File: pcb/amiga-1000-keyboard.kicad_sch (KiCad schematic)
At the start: 113 parts, among them J1 KEYBOARD, Q1 NPN, SW1 ESC, SW10 F9, SW11 F10, SW12 HELP, SW13 `, SW14 1, SW15 2, SW16 3, SW17 4, SW18 5, SW19 6, SW2 F1, SW20 7, SW21 8, SW22 9, SW23 0, SW24 -, SW25 =, SW26 \, SW27 UP, SW28 TAB, SW29 Q, SW3 F2, SW30 W, SW31 E, SW32 R, SW33 T, SW34 Y, SW35 U, SW36 I, SW37 O, SW38 P, SW39 [, SW4 F3, SW40 ], SW41 RETURN, SW42 LEFT, SW43 CAPS LOCK, SW44 A, SW45 S, SW46 D, SW47 F, SW48 G, SW49 H, SW5 F4, SW50 J, SW51 K, SW52 L, SW53 ;, SW54 ', SW55 (RET) INTL, SW56 DEL, SW57 RIGHT, SW58 L SHIFT INTL, SW59 Z, SW6 F5, SW60 X, SW61 C, SW62 V, SW63 B, SW64 N, SW65 M, SW66 ,, SW67 ., SW68 /, SW69 SPACE, SW7 F6, SW70 BACKSPACE, SW71 DOWN, SW72 KP 9, SW73 KP 6, SW74 KP 3, SW75 KP ., SW76 KP 8, SW77 KP 5, SW78 KP 2, SW79 KP ENTER, SW8 F7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

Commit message: assign footprints, set the 3mhz crystal and add the iso shift switch.
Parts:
- added SW92: L SHIFT ISO, amiga1000:Mitsumi_A1000_Switch, symbol Switch:SW_Push
- C1, C2, C3, C4, C6, C7, C9: footprint (none) -> Capacitor_THT:C_Disc_D5.0mm_W2.5mm_P5.00mm
- C5: value 1uF -> 1uF 25V tant; footprint (none) -> Capacitor_THT:CP_Radial_Tantal_D4.5mm_P2.50mm; symbol Device:C -> Device:C_Polarized
- C8: footprint (none) -> Capacitor_THT:CP_Radial_D5.0mm_P2.00mm
- D1: footprint (none) -> Diode_THT:D_DO-35_SOD27_P7.62mm_Horizontal
- D2: footprint (none) -> amiga1000:Mitsumi_A1000_CapsLock_LED
- FB1, FB2, FB3: footprint (none) -> Inductor_THT:L_Axial_L9.5mm_D4.0mm_P12.70mm_Horizontal_Fastron_SMCC
- J1: footprint (none) -> Connector_PinHeader_2.54mm:PinHeader_1x04_P2.54mm_Vertical
- Q1: footprint (none) -> amiga1000:TO-92_Inline_ECB
- R1, R2, R3: footprint (none) -> Resistor_THT:R_Axial_DIN0207_L6.3mm_D2.5mm_P10.16mm_Horizontal
- SW1, SW10, SW11, SW12, SW13, SW14, SW15, SW16, SW17, SW18, SW19, SW2, SW20, SW21, SW22, SW23, SW24, SW25, SW26, SW27, SW28, SW29, SW3, SW30, SW31, SW32, SW33, SW34, SW35, SW36, SW37, SW38, SW39, SW4, SW40, SW41, SW42, SW43, SW44, SW45, SW46, SW47, SW48, SW49, SW5, SW50, SW51, SW52, SW53, SW54, SW56, SW57, SW59, SW6, SW60, SW61, SW62, SW63, SW64, SW65, SW66, SW67, SW68, SW69, SW7, SW70, SW71, SW72, SW73, SW74, SW75, SW76, SW77, SW78, SW79, SW8, SW80, SW81, SW82, SW83, SW84, SW85, SW86, SW87, SW88, SW89, SW9, SW90, SW91: footprint (none) -> amiga1000:Mitsumi_A1000_Switch
- SW55, SW58: footprint (none) -> amiga1000:Mitsumi_A1000_Switch; now not fitted
- U2: footprint (none) -> Package_DIP:DIP-14_W7.62mm
- Y1: value XTAL -> 3.000MHz; footprint (none) -> Crystal:Crystal_HC49-U_Vertical
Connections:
- net GND: now also SW92.2
- net PB4: now also SW92.1
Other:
- note added: "3.000 MHz: not marked on the drawing, read from the crystal on an assembled board."
- note removed: "Crystal frequency not marked on the drawing - verify on an original board."

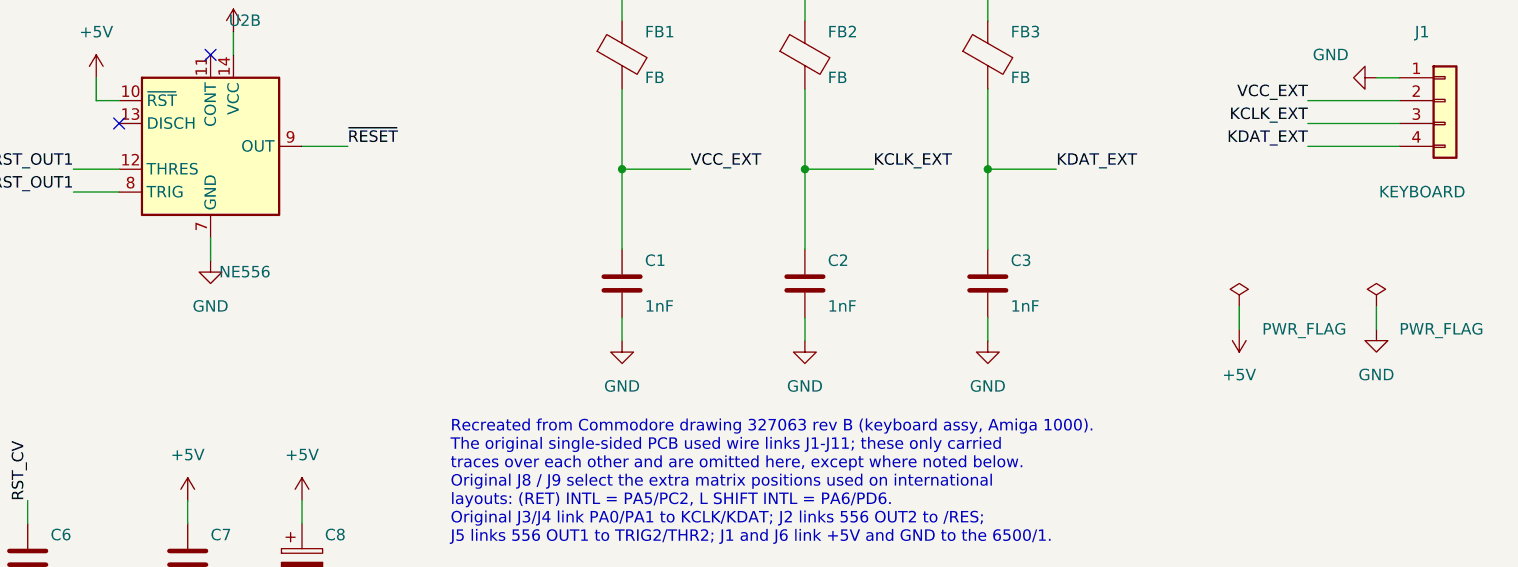
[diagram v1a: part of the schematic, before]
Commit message: mark the unfitted cable filter caps c1-c3 do not populate.
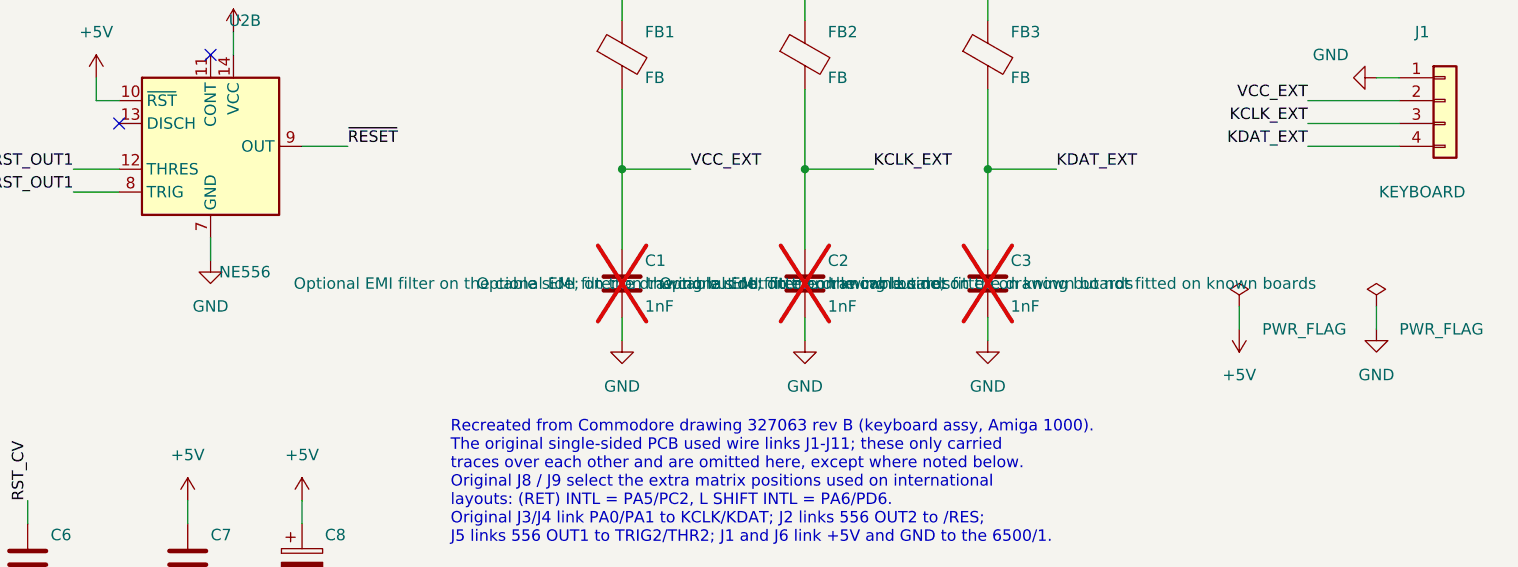
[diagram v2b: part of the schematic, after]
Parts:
- C1, C2, C3: now not fitted
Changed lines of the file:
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@@
 		(on_board yes)
 		(in_pos_files yes)
-		(dnp no)
+		(dnp yes)
 		(property "Reference" "C2"
 			(at 325.12 218.44 0)
@@
 			)
 		)
-		(property "Description" ""
+		(property "Description" "Optional EMI filter on the cable side; on the drawing but not fitted on known boards"
 			(at 322.58 220.98 0)
 			(show_name no)
@@
 		(on_board yes)
 		(in_pos_files yes)
-		(dnp no)
+		(dnp yes)
 		(property "Reference" "C3"
 			(at 345.44 218.44 0)
@@
 			)
 		)
-		(property "Description" ""
+		(property "Description" "Optional EMI filter on the cable side; on the drawing but not fitted on known boards"
 			(at 342.9 220.98 0)
 			(show_name no)
@@
 		(on_board yes)
 		(in_pos_files yes)
-		(dnp no)
+		(dnp yes)
 		(property "Reference" "C1"
 			(at 304.8 218.44 0)
@@
 			)
 		)
-		(property "Description" ""
+		(property "Description" "Optional EMI filter on the cable side; on the drawing but not fitted on known boards"
 			(at 302.26 220.98 0)
 			(show_name no)

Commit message: add part fields and a bom generated from the schematic.
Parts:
- added H1, H2, H3, H4, H5, H6, H7, H8, H9: Plate GND, amiga1000:MountingHole_3.8mm_Plate_GND, symbol Mechanical:MountingHole_Pad
- C1, C2, C3: Part (none) -> 1nF 50V ceramic disc, 5 mm
- C4, C7: Part (none) -> 100nF 50V ceramic disc, 5 mm
- C5: Part (none) -> 1uF 25V tantalum, 2.5 mm
- C6: Part (none) -> 10nF 50V ceramic disc, 5 mm
- C8: Part (none) -> 47uF 16V electrolytic, 5 mm dia, 2 mm
- C9: Part (none) -> 22pF 50V C0G ceramic disc, 5 mm
- D1: Part (none) -> 1N4148 small-signal diode, DO-35
- D2: Part (none) -> LED built into the Caps Lock switch (no separate part)
- FB1, FB2, FB3: Part (none) -> Axial ferrite bead, e.g. Fair-Rite 2743001112
- J1: Part (none) -> Original 4-wire cable soldered in (or a 1x4 2.54 mm header)
- Q1: value NPN -> 2SC2021; footprint amiga1000:TO-92_Inline_ECB -> amiga1000:TO-92_Inline_Wide_ECB; Part (none) -> 2SC2021 (Rohm SPT, original) or 2SC1815/KSC1815 TO-92; any 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
- R1: Part (none) -> 150R 1/4W axial
- R2: Part (none) -> 510K 1/4W axial
- R3: Part (none) -> 560K 1/4W axial
- SW1, SW10, SW11, SW12, SW13, SW14, SW15, SW16, SW17, SW18, SW19, SW2, SW20, SW21, SW22, SW23, SW24, SW25, SW26, SW27, SW28, SW29, SW3, SW30, SW31, SW32, SW33, SW34, SW35, SW36, SW37, SW38, SW39, SW4, SW40, SW41, SW42, SW43, SW44, SW45, SW46, SW47, SW48, SW49, SW5, SW50, SW51, SW52, SW53, SW54, SW55, SW56, SW57, SW58, SW59, SW6, SW60, SW61, SW62, SW63, SW64, SW65, SW66, SW67, SW68, SW69, SW7, SW70, SW71, SW72, SW73, SW74, SW75, SW76, SW77, SW78, SW79, SW8, SW80, SW81, SW82, SW83, SW84, SW85, SW86, SW87, SW88, SW89, SW9, SW90, SW91, SW92: Part (none) -> Mitsumi standard mechanical Type 2 (KCT) keyswitch, salvaged
- U1: Part (none) -> Commodore 6500/1 keyboard controller, salvaged from an A100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
- U2: Part (none) -> NE556N dual timer, DIP-14
- Y1: Part (none) -> 3.000 MHz crystal, HC-49/U
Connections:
- net GND: now also H1.1, H2.1, H3.1, H4.1, H5.1, H6.1, H7.1, H8.1, H9.1
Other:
- note added: "Plate screw holes: plated, tied to GND to ground the steel key plate"

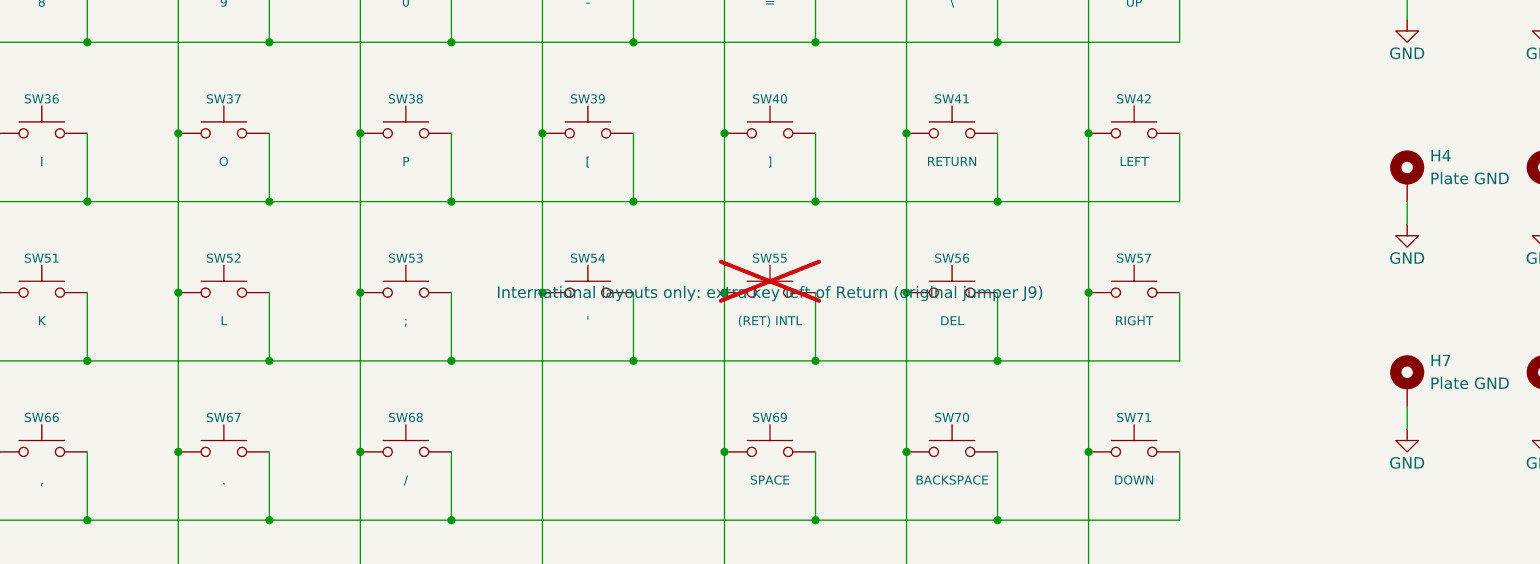
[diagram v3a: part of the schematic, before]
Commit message: turn the return switch round and fit sw55 as the dummy support housing.
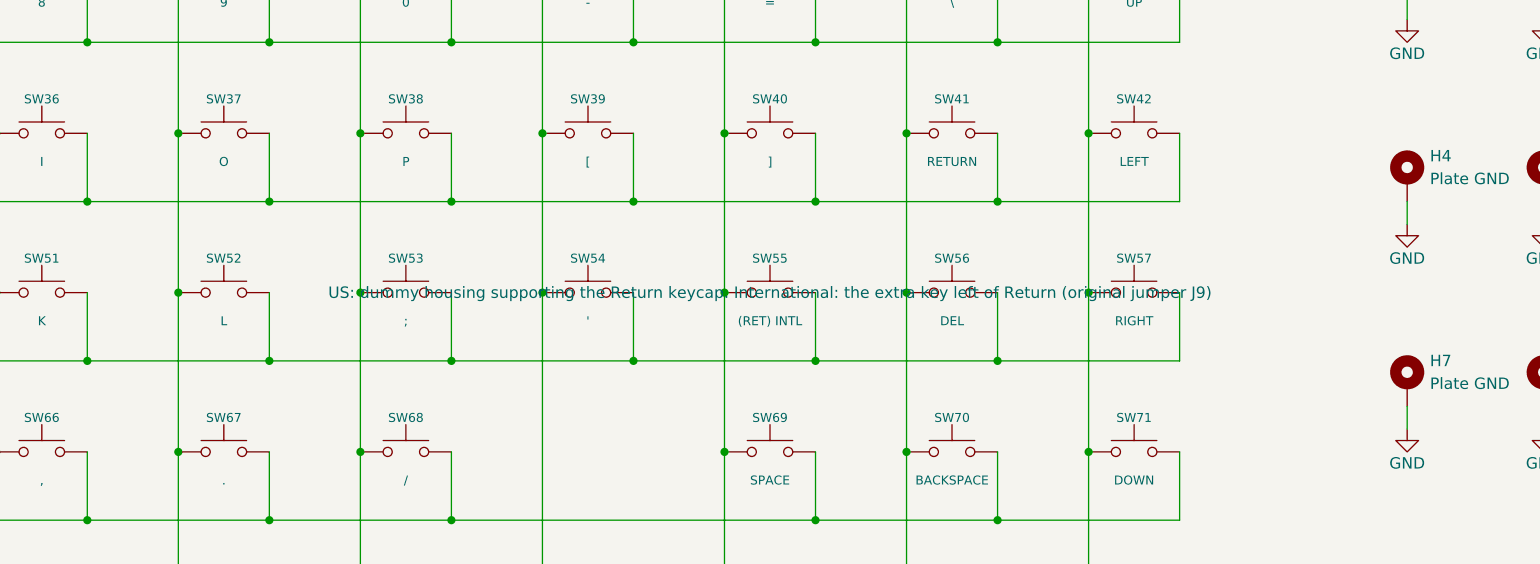
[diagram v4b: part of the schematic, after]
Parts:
- D1: Part 1N4148 small-signal diode, DO-35 -> 1N4148 small-signal diode, DO-35 (original: unmarked glass,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
- SW55: Part Mitsumi standard mechanical Type 2 (KCT) keyswitch, salvaged -> Dummy Mitsumi housing (one leg, no spring) supporting the R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; now fitted
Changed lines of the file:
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@@
 		(on_board yes)
 		(in_pos_files yes)
-		(dnp yes)
+		(dnp no)
 		(property "Reference" "SW55"
 			(at 289.56 87.63 0)
@@
 			)
 		)
-		(property "Description" "International layouts only: extra key left of Return (original jumper J9)"
+		(property "Description" "US: dummy housing supporting the Return keycap. International: the extra key left of Return (original jumper J9)"
 			(at 289.56 91.44 0)
 			(show_name no)
@@
 			)
 		)
-		(property "Part" "Mitsumi standard mechanical Type 2 (KCT) keyswitch, salvaged"
+		(property "Part" "Dummy Mitsumi housing (one leg, no spring) supporting the Return keycap on US layouts; a real switch on international layouts"
 			(at 289.56 91.44 0)
 			(hide yes)
@@
 			)
 		)
-		(property "Part" "1N4148 small-signal diode, DO-35"
+		(property "Part" "1N4148 small-signal diode, DO-35 (original: unmarked glass, yellow cathode band, likely a 1S1588)"
 			(at 170.18 251.46 0)
 			(hide yes)

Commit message: lay y1 flat on the board, can towards the keys, as on the original.
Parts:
- Y1: footprint Crystal:Crystal_HC49-U_Vertical -> Crystal:Crystal_HC49-U_Horizontal
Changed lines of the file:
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@@
 			)
 		)
-		(property "Footprint" "Crystal:Crystal_HC49-U_Vertical"
+		(property "Footprint" "Crystal:Crystal_HC49-U_Horizontal"
 			(at 50.8 182.88 0)
 			(hide yes)
